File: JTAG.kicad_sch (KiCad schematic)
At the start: 33 parts, among them J1201 DX07S016JA1R1500, SW1201 SW_Push, SW201 SW_Push, U1201 RP2040, U1203 W25Q16JVSS, Y201 12MHz

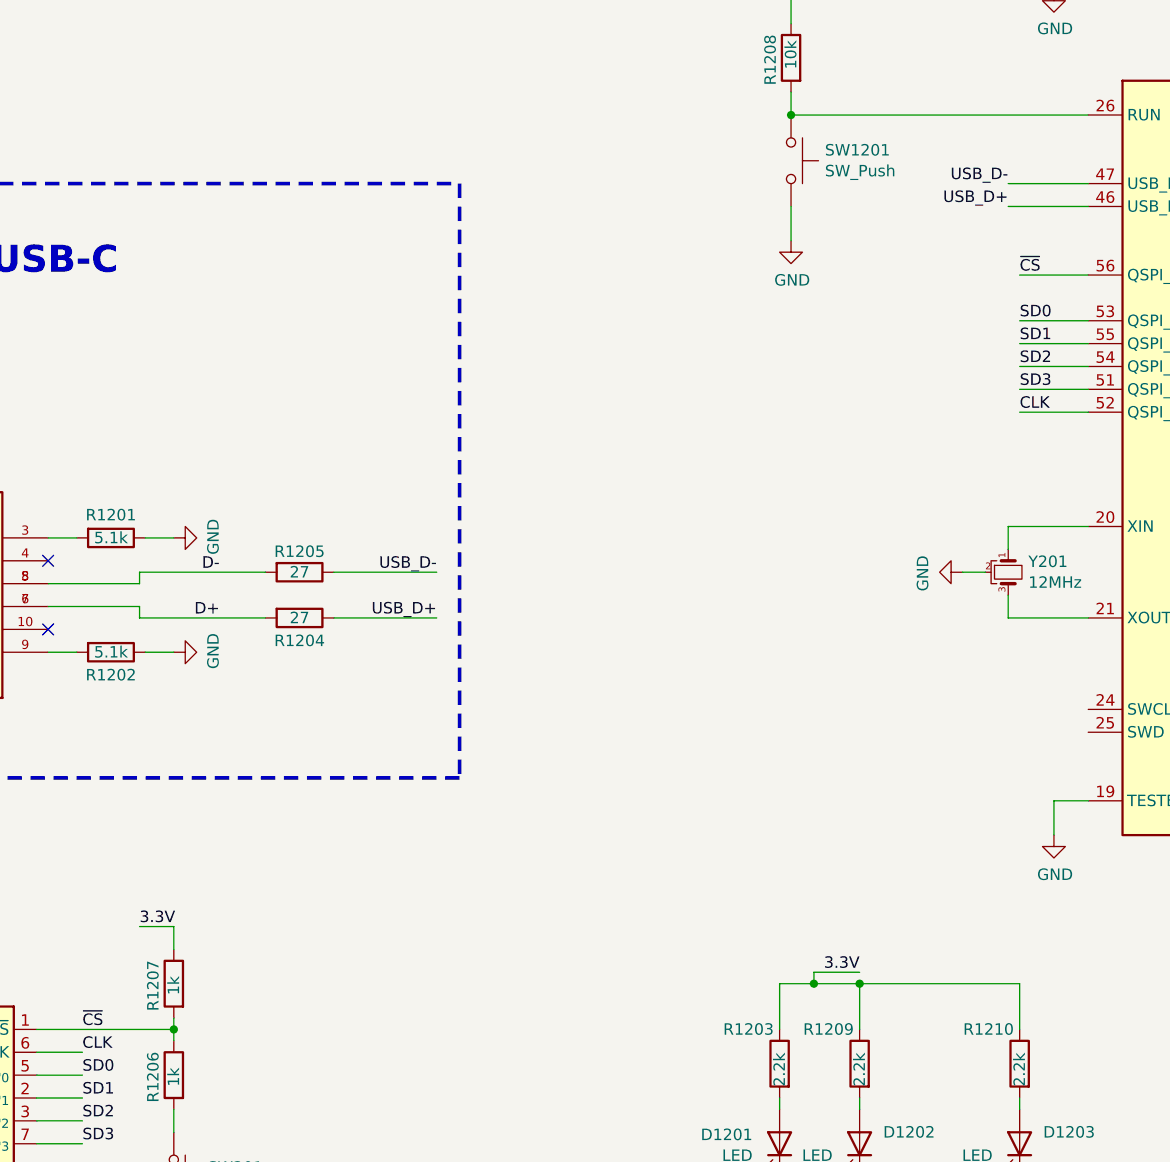
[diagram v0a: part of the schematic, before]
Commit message: Fix mistakes in V1.0
Signed-off-by: Alexis Jeandet <alexis.jeandet@member.fsf.org>
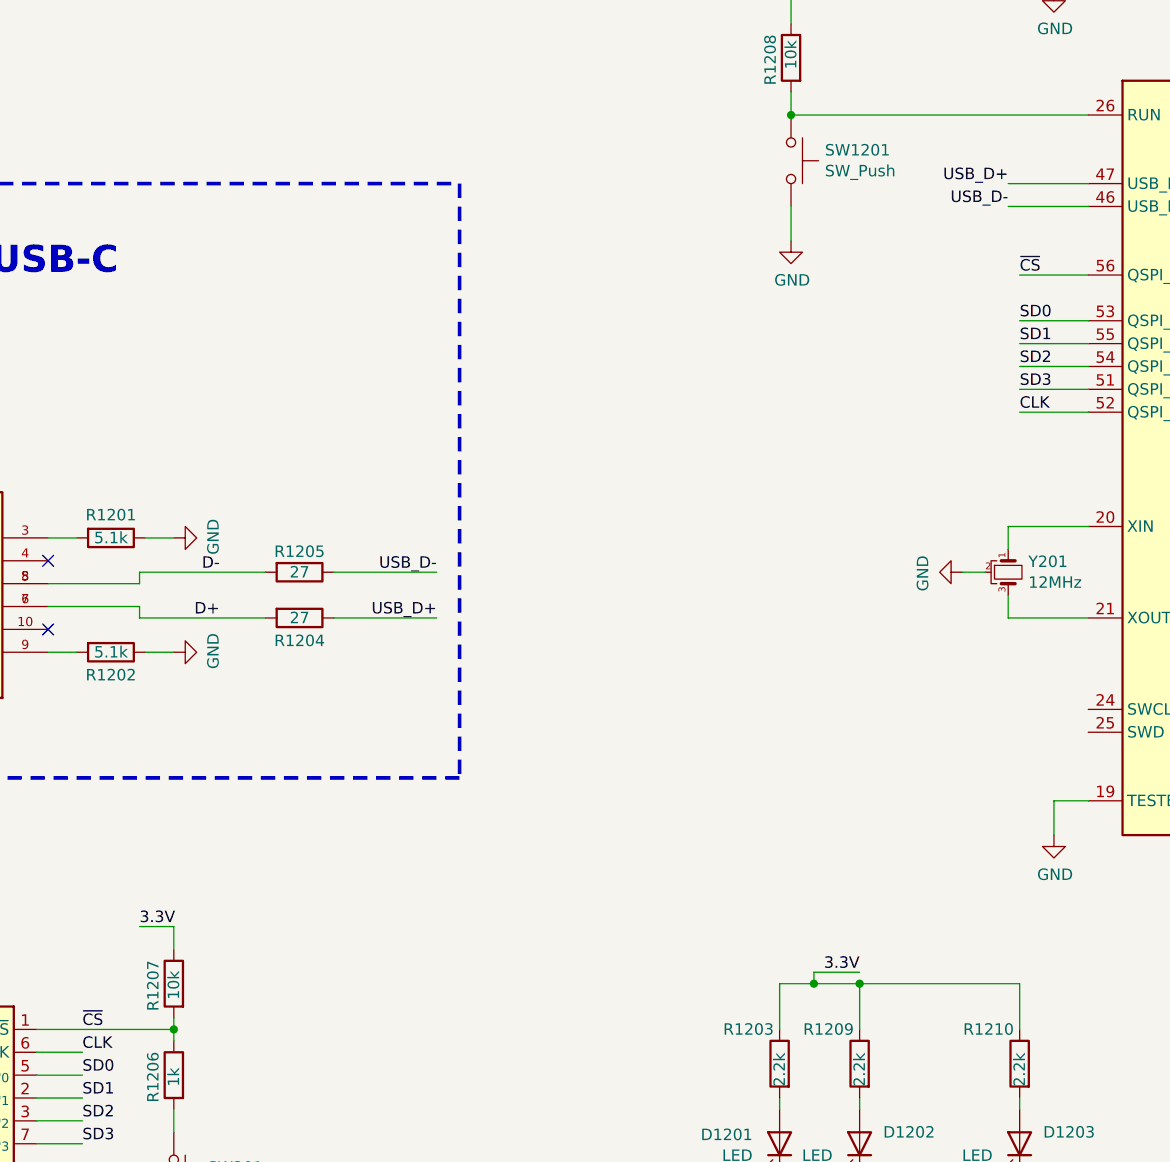
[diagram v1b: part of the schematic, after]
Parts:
- R1207: value 1k -> 10k
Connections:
- net USB_D+: now also U1201.47 (USB_DP); no longer U1201.46 (USB_DM)
- net USB_D-: now also U1201.46 (USB_DM); no longer U1201.47 (USB_DP)
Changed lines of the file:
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@@
 	)
 	(label "USB_D-"
-		(at 158.75 59.69 180)
+		(at 158.75 62.23 180)
 		(effects
 			(font
@@
 	)
 	(label "USB_D+"
-		(at 158.75 62.23 180)
+		(at 158.75 59.69 180)
 		(effects
 			(font
@@
 			)
 		)
-		(property "Value" "1k"
-			(at 66.04 149.86 90)
-			(effects
-				(font
+		(property "Value" "10k"
+			(at 66.04 150.368 90)
+			(effects
+				(font
